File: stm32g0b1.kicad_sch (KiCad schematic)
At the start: 7 parts, among them J1 Conn_ST_STDC14, J3 Conn_01x13, U5 STM32L432KBUx

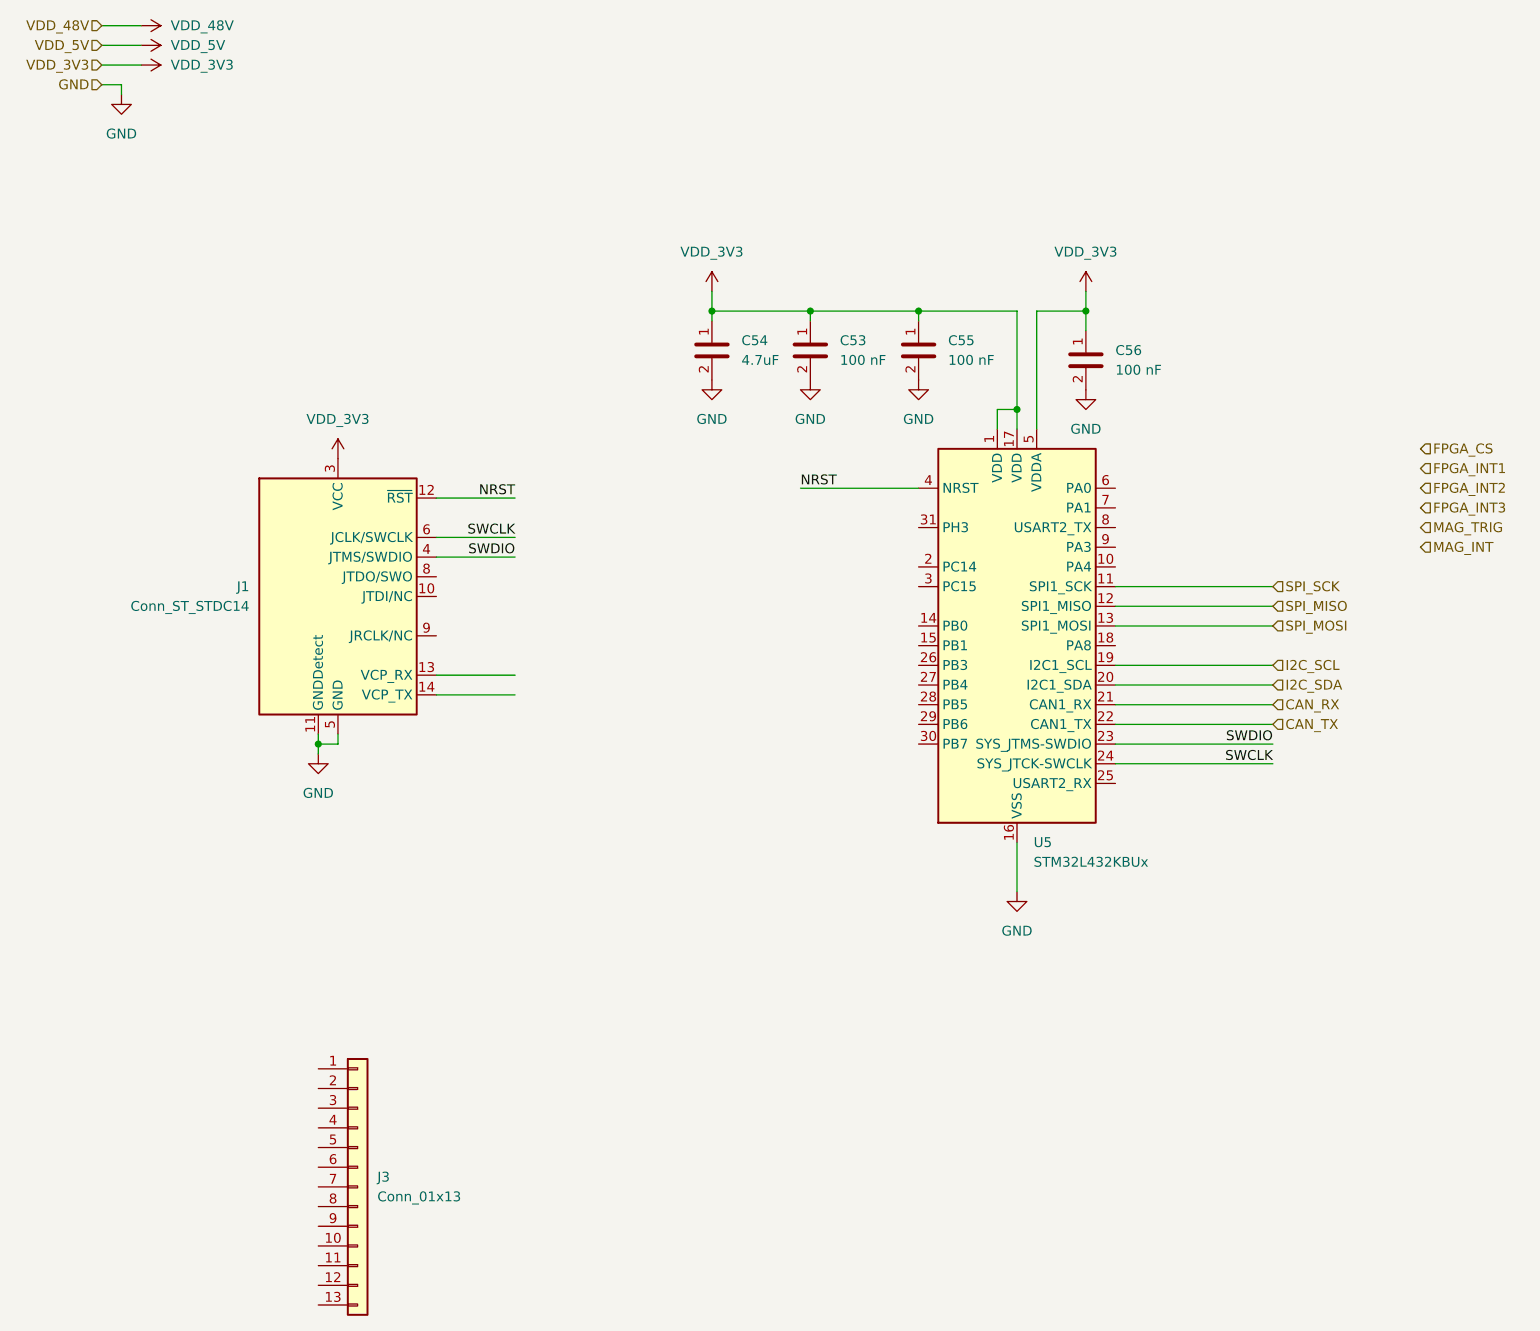
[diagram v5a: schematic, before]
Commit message: fix: finalized position of fpc programmer
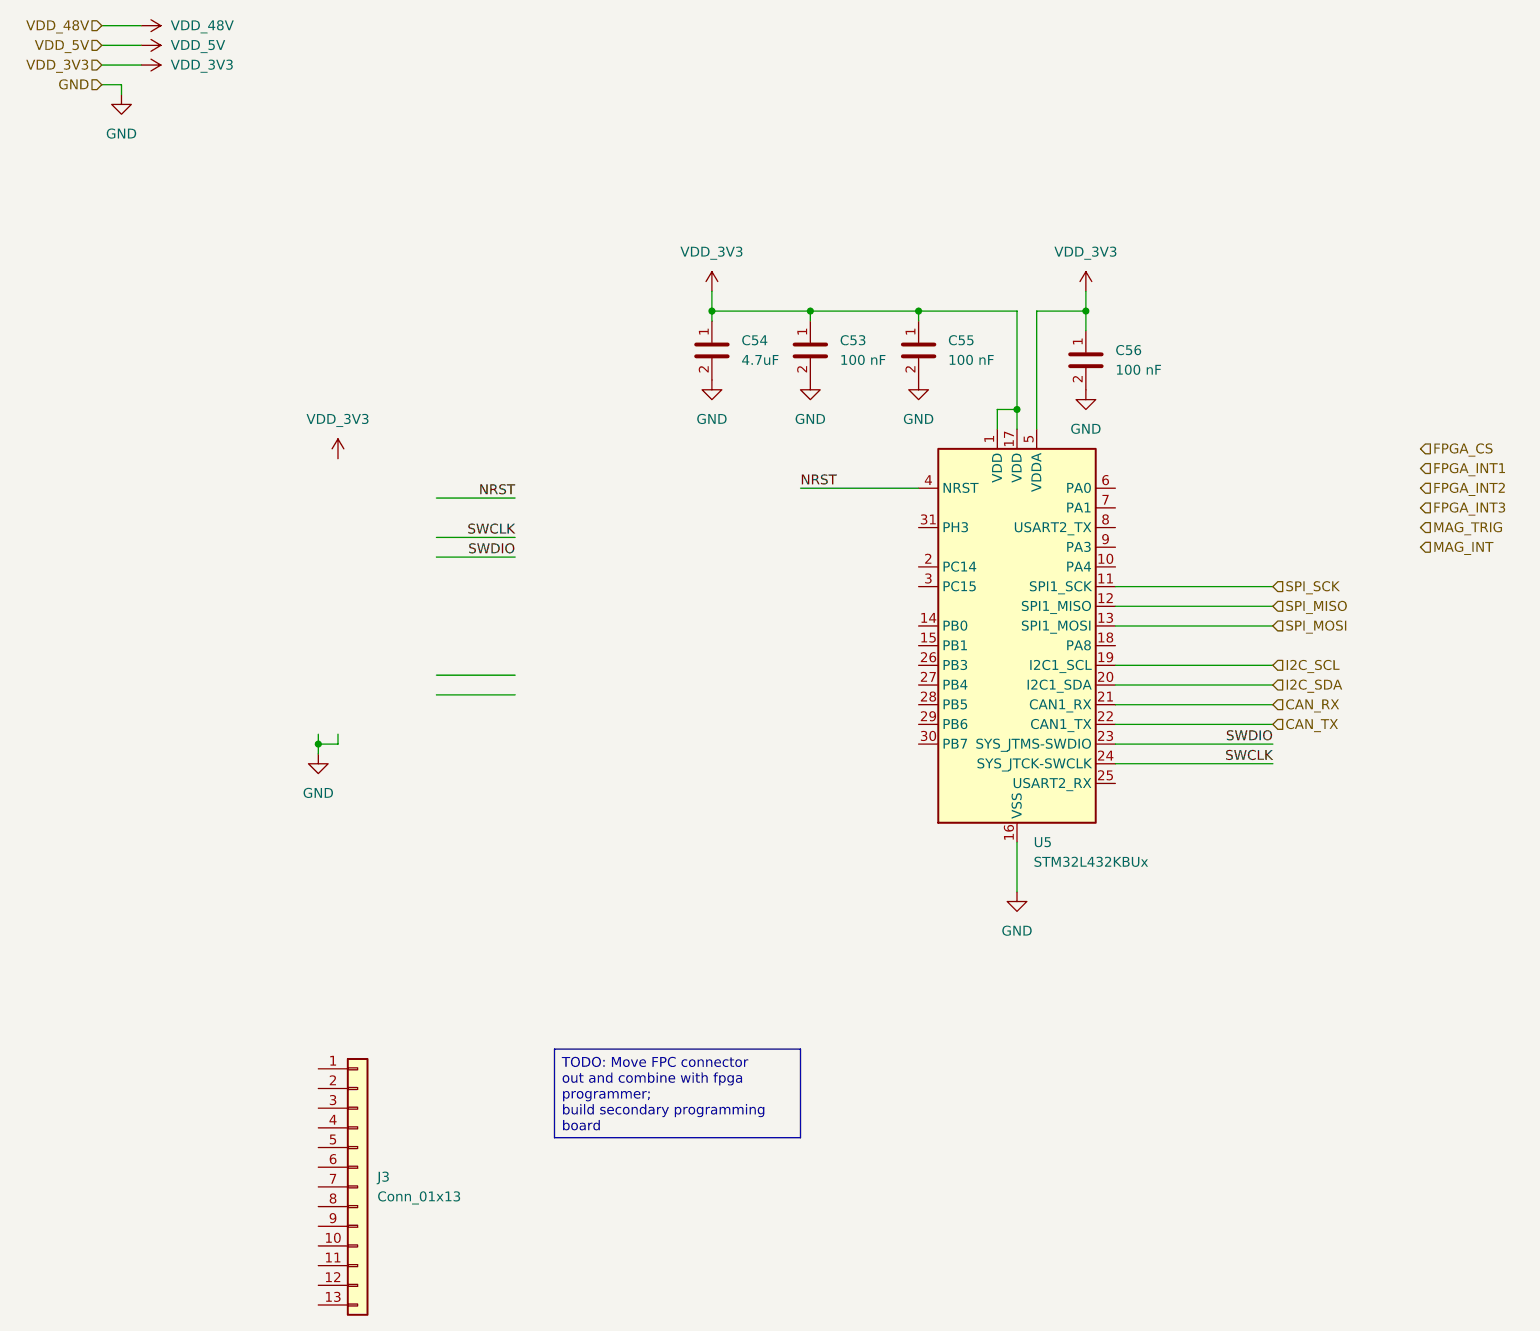
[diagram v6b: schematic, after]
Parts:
- removed J1: Conn_ST_STDC14, Connector_FFC-FPC:Molex_502231-1500_1x15-1SH_P0.5mm_Vertical, symbol Connector:Conn_ST_STDC14
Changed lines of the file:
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@@
 	(generator_version "9.0")
 	(paper "A4")
+	(text_box "TODO: Move FPC connector out and combine with fpga programmer;\nbuild secondary programming board"
+		(exclude_from_sim no)
+		(at 82.55 148.59 0)
+		(size 31.75 11.43)
+		(margins 0.9525 0.9525 0.9525 0.9525)
+		(stroke
+			(width 0)
+			(type solid)
+		)
+		(fill
+			(type none)
+		)
+		(effects
+			(font
+				(size 1.27 1.27)
+			)
+			(justify left top)
+		)
+	)
 	(junction
 		(at 115.57 53.34)
@@
 					(unit 1)
 				)
-			)
-		)
-	)
-	(symbol
-		(lib_id "Connector:Conn_ST_STDC14")
-		(at 54.61 90.17 0)
-		(unit 1)
-		(exclude_from_sim no)
-		(in_bom yes)
-		(on_board yes)
-		(dnp no)
-		(fields_autoplaced yes)
-		(property "Reference" "J1"
-			(at 43.18 88.8999 0)
-			(effects
-				(font
-					(size 1.27 1.27)
-				)
-				(justify right)
-			)
-		)
-		(property "Value" "Conn_ST_STDC14"
-			(at 43.18 91.4399 0)
-			(effects
-				(font
-					(size 1.27 1.27)
-				)
-				(justify right)
-			)
-		)
-		(property "Footprint" "Connector_FFC-FPC:Molex_502231-1500_1x15-1SH_P0.5mm_Vertical"
-			(at 54.61 90.17 0)
-			(effects
-				(font
-					(size 1.27 1.27)
-				)
-				(hide yes)
-			)
-		)
-		(property "Datasheet" "https://www.st.com/content/ccc/resource/technical/document/user_manual/group1/99/49/91/b6/b2/3a/46/e5/DM00526767/files/DM00526767.pdf/jcr:content/translations/en.DM00526767.pdf"
-			(at 45.72 121.92 90)
-			(effects
-				(font
-					(size 1.27 1.27)
-				)
-				(hide yes)
-			)
-		)
-		(property "Description" "ST Debug Connector, standard ARM Cortex-M SWD and JTAG interface plus UART"
-			(at 54.61 90.17 0)
-			(effects
-				(font
-					(size 1.27 1.27)
-				)
-				(hide yes)
-			)
-		)
-		(property "MFR_PN1" ""
-			(at 54.61 90.17 0)
-			(effects
-				(font
-					(size 1.27 1.27)
-				)
-				(hide yes)
-			)
-		)
-		(property "MFR_PN2" ""
-			(at 54.61 90.17 0)
-			(effects
-				(font
-					(size 1.27 1.27)
-				)
-				(hide yes)
-			)
-		)
-		(property "MFR_PN3" ""
-			(at 54.61 90.17 0)
-			(effects
-				(font
-					(size 1.27 1.27)
-				)
-				(hide yes)
-			)
-		)
-		(property "JLC_PN" ""
-			(at 54.61 90.17 0)
-			(effects
-				(font
-					(size 1.27 1.27)
-				)
-				(hide yes)
-			)
-		)
-		(pin "11"
-		)
-		(pin "1"
-		)
-		(pin "7"
-		)
-		(pin "2"
-		)
-		(pin "12"
-		)
-		(pin "3"
-		)
-		(pin "8"
-		)
-		(pin "5"
-		)
-		(pin "10"
-		)
-		(pin "6"
-		)
-		(pin "14"
-		)
-		(pin "4"
-		)
-		(pin "9"
-		)
-		(pin "13"
-		)
-		(instances
-			(project "kicad-template-project"
-				(path "/e1f256b3-686f-4e34-9512-fa5de8536fd7/0cb427d4-6402-4c72-8ad8-57931fc8c658"
-					(reference "J1")
-					(unit 1)
-				)
